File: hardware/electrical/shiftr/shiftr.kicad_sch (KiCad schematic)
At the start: 1 part

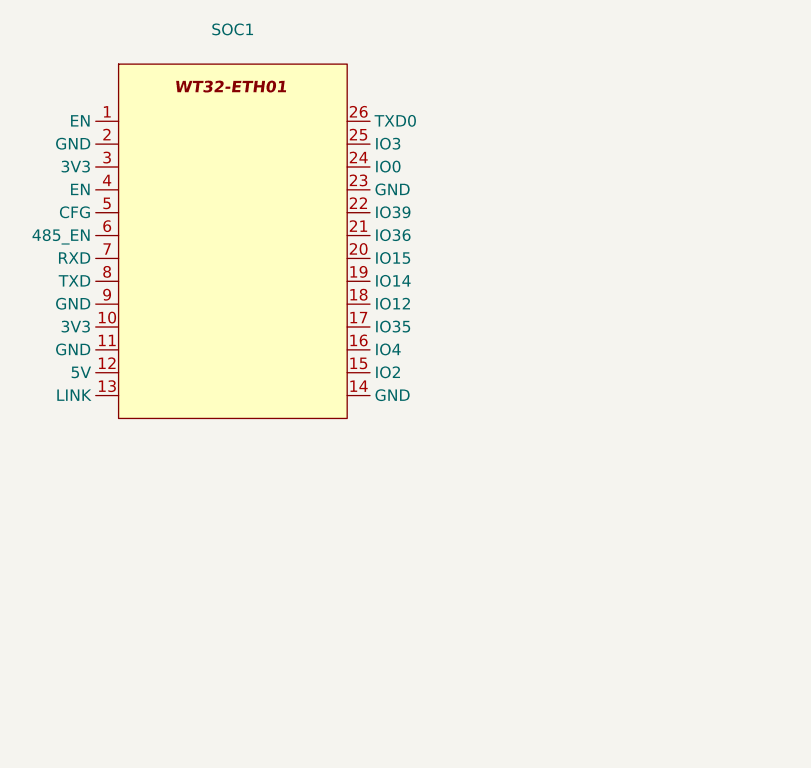
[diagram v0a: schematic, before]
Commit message: add audio jack sch and pcb
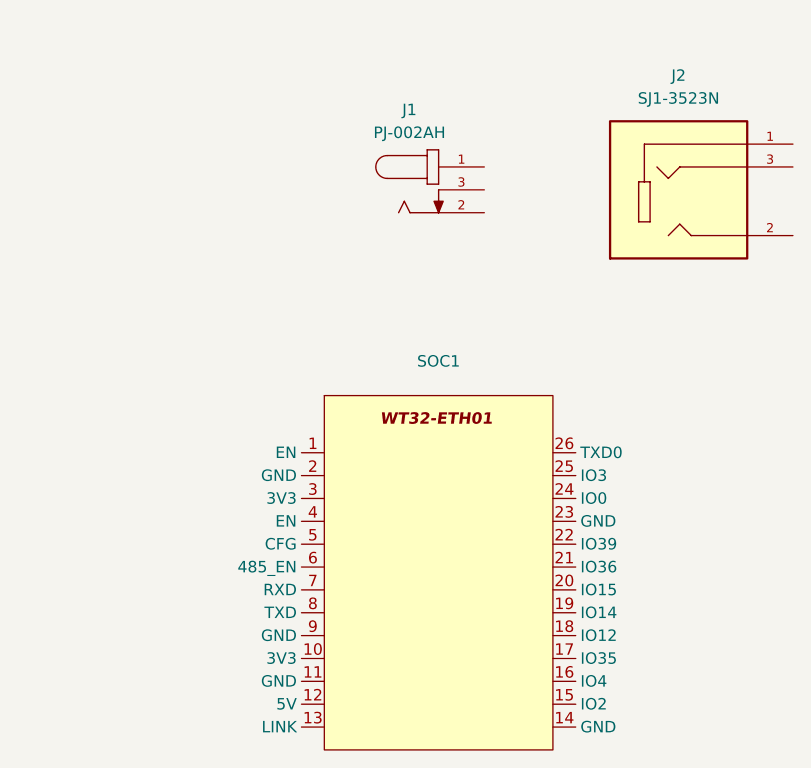
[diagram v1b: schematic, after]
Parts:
- added J1: PJ-002AH, footprint_library:PJ-002AH, symbol symbol_library:PJ-002AH
- added J2: SJ1-3523N, footprint_library:CUI_SJ1-3523N, symbol symbol_library:SJ1-3523N
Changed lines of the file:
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@@
 	(paper "A4")
 	(symbol
+		(lib_id "symbol_library:PJ-002AH")
+		(at 69.85 45.72 0)
+		(unit 1)
+		(exclude_from_sim no)
+		(in_bom yes)
+		(on_board yes)
+		(dnp no)
+		(fields_autoplaced yes)
+		(property "Reference" "J1"
+			(at 66.6143 36.83 0)
+			(effects
+				(font
+					(size 1.27 1.27)
+				)
+			)
+		)
+		(property "Value" "PJ-002AH"
+			(at 66.6143 39.37 0)
+			(effects
+				(font
+					(size 1.27 1.27)
+				)
+			)
+		)
+		(property "Footprint" "footprint_library:PJ-002AH"
+			(at 72.898 58.166 0)
+			(effects
+				(font
+					(size 1.27 1.27)
+				)
+				(justify bottom)
+				(hide yes)
+			)
+		)
+		(property "Datasheet" "https://www.sameskydevices.com/product/resource/pj-002ah.pdf"
+			(at 73.66 36.83 0)
+			(effects
+				(font
+					(size 1.27 1.27)
+				)
+				(hide yes)
+			)
+		)
+		(property "Description" "BARREL JACK 2.1 X 5.5"
+			(at 71.374 34.544 0)
+			(effects
+				(font
+					(size 1.27 1.27)
+				)
+				(hide yes)
+			)
+		)
+		(property "MANUFACTURER" "CUI INC"
+			(at 72.898 54.61 0)
+			(effects
+				(font
+					(size 1.27 1.27)
+				)
+				(justify bottom)
+				(hide yes)
+			)
+		)
+		(property "STANDARD" "Manufacturer recommendations"
+			(at 72.39 56.134 0)
+			(effects
+				(font
+					(size 1.27 1.27)
+				)
+				(justify bottom)
+				(hide yes)
+			)
+		)
+		(pin "1"
+		)
+		(pin "2"
+		)
+		(pin "3"
+		)
+		(instances
+			(project ""
+				(path "/3bfa63c6-9d72-4aec-ae9c-b2577824d50b"
+					(reference "J1")
+					(unit 1)
+				)
+			)
+		)
+	)
+	(symbol
+		(lib_id "symbol_library:SJ1-3523N")
+		(at 96.52 45.72 0)
+		(unit 1)
+		(exclude_from_sim no)
+		(in_bom yes)
+		(on_board yes)
+		(dnp no)
+		(fields_autoplaced yes)
+		(property "Reference" "J2"
+			(at 96.52 33.02 0)
+			(effects
+				(font
+					(size 1.27 1.27)
+				)
+			)
+		)
+		(property "Value" "SJ1-3523N"
+			(at 96.52 35.56 0)
+			(effects
+				(font
+					(size 1.27 1.27)
+				)
+			)
+		)
+		(property "Footprint" "footprint_library:CUI_SJ1-3523N"
+			(at 101.854 59.436 0)
+			(effects
+				(font
+					(size 1.27 1.27)
+				)
+				(justify bottom)
+				(hide yes)
+			)
+		)
+		(property "Datasheet" "https://www.sameskydevices.com/product/resource/sj1-352xn.pdf"
+			(at 96.012 67.818 0)
+			(effects
+				(font
+					(size 1.27 1.27)
+				)
+				(hide yes)
+			)
+		)
+		(property "Description" "AUDIO JACK 3.5MM 3P"
+			(at 96.52 45.72 0)
+			(effects
+				(font
+					(size 1.27 1.27)
+				)
+				(hide yes)
+			)
+		)
+		(property "PARTREV" "1.05"
+			(at 97.028 64.008 0)
+			(effects
+				(font
+					(size 1.27 1.27)
+				)
+				(justify bottom)
+				(hide yes)
+			)
+		)
+		(property "STANDARD" "Manufacturer Recommendations"
+			(at 97.282 57.658 0)
+			(effects
+				(font
+					(size 1.27 1.27)
+				)
+				(justify bottom)
+				(hide yes)
+			)
+		)
+		(property "MAXIMUM_PACKAGE_HEIGHT" "6.25 mm"
+			(at 97.282 66.294 0)
+			(effects
+				(font
+					(size 1.27 1.27)
+				)
+				(justify bottom)
+				(hide yes)
+			)
+		)
+		(property "MANUFACTURER" "CUI Devices"
+			(at 96.774 62.484 0)
+			(effects
+				(font
+					(size 1.27 1.27)
+				)
+				(justify bottom)
+				(hide yes)
+			)
+		)
+		(pin "1"
+		)
+		(pin "3"
+		)
+		(pin "2"
+		)
+		(instances
+			(project ""
+				(path "/3bfa63c6-9d72-4aec-ae9c-b2577824d50b"
+					(reference "J2")
+					(unit 1)
+				)
+			)
+		)
+	)
+	(symbol
 		(lib_id "symbol_library:WT32-ETH01")
-		(at 46.99 59.69 0)
+		(at 69.85 96.52 0)
 		(unit 1)
 		(exclude_from_sim no)
@@
 		(fields_autoplaced yes)
 		(property "Reference" "SOC1"
-			(at 46.99 27.94 0)
+			(at 69.85 64.77 0)
 			(effects
 				(font
@@
 		)
 		(property "Value" "~"
-			(at 46.99 30.48 0)
+			(at 69.85 67.31 0)
 			(effects
 				(font
@@
 		)
 		(property "Footprint" "footprint_library:WT32-ETH01"
-			(at 46.99 59.69 0)
+			(at 69.85 96.52 0)
 			(effects
 				(font
@@
 		)
 		(property "Datasheet" "kicad-embed://WT32-ETH01_datasheet_V1.1- en.pdf"
-			(at 46.99 59.69 0)
-			(effects
-				(font
-					(size 1.27 1.27)
-				)
-				(hide yes)
-			)
-		)
-		(property "Description" ""
-			(at 46.99 59.69 0)
-			(effects
-				(font
-					(size 1.27 1.27)
-				)
-				(hide yes)
-			)
+			(at 69.85 96.52 0)
+			(effects
+				(font
+					(size 1.27 1.27)
+				)
+				(hide yes)
+			)
+		)
+		(property "Description" "ARDUINO"
+			(at 69.85 96.52 0)
+			(effects
+				(font
+					(size 1.27 1.27)
+				)
+				(hide yes)
+			)
+		)
+		(pin "21"
+		)
+		(pin "1"
+		)
+		(pin "3"
+		)
+		(pin "2"
+		)
+		(pin "10"
+		)
+		(pin "13"
+		)
+		(pin "25"
+		)
+		(pin "23"
+		)
+		(pin "11"
+		)
+		(pin "9"
+		)
+		(pin "24"
 		)
 		(pin "22"
 		)
+		(pin "4"
+		)
+		(pin "6"
+		)
+		(pin "7"
+		)
+		(pin "5"
+		)
+		(pin "8"
+		)
+		(pin "12"
+		)
+		(pin "26"
+		)
 		(pin "19"
 		)
-		(pin "21"
-		)
-		(pin "26"
-		)
-		(pin "23"
-		)
-		(pin "2"
-		)
-		(pin "7"
-		)
-		(pin "10"
-		)
-		(pin "9"
+		(pin "17"
+		)
+		(pin "18"
 		)
 		(pin "16"
 		)
-		(pin "11"
-		)
-		(pin "24"
-		)
-		(pin "3"
-		)
-		(pin "12"
-		)
-		(pin "18"
-		)
-		(pin "5"
+		(pin "15"
+		)
+		(pin "20"
 		)
 		(pin "14"
 		)
-		(pin "20"
-		)
-		(pin "6"
-		)
-		(pin "25"
-		)
-		(pin "4"
-		)
-		(pin "17"
-		)
-		(pin "1"
-		)
-		(pin "15"
-		)
-		(pin "8"
-		)
-		(pin "13"
-		)
 		(instances

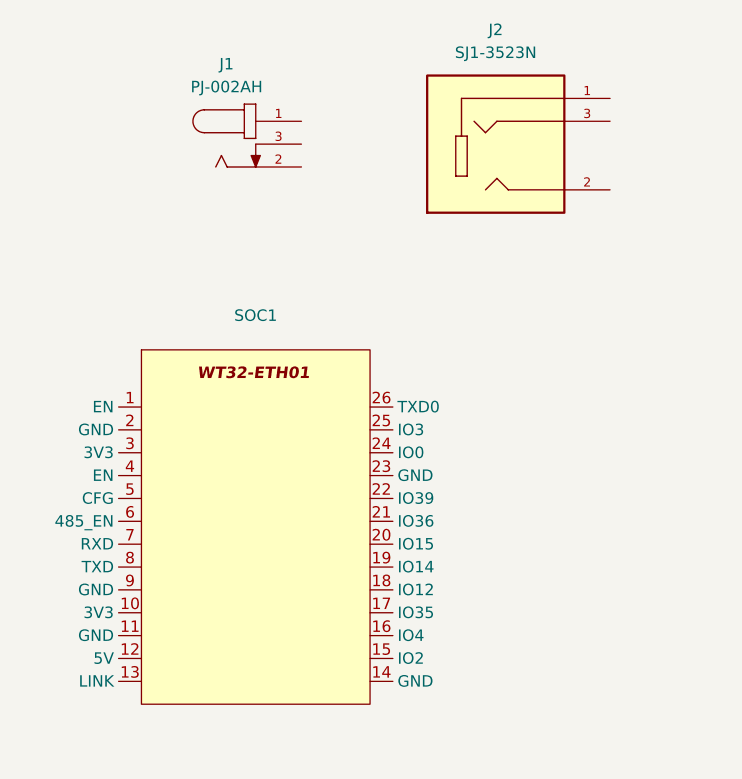
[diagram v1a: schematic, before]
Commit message: add usb c connector sch and pcb lib
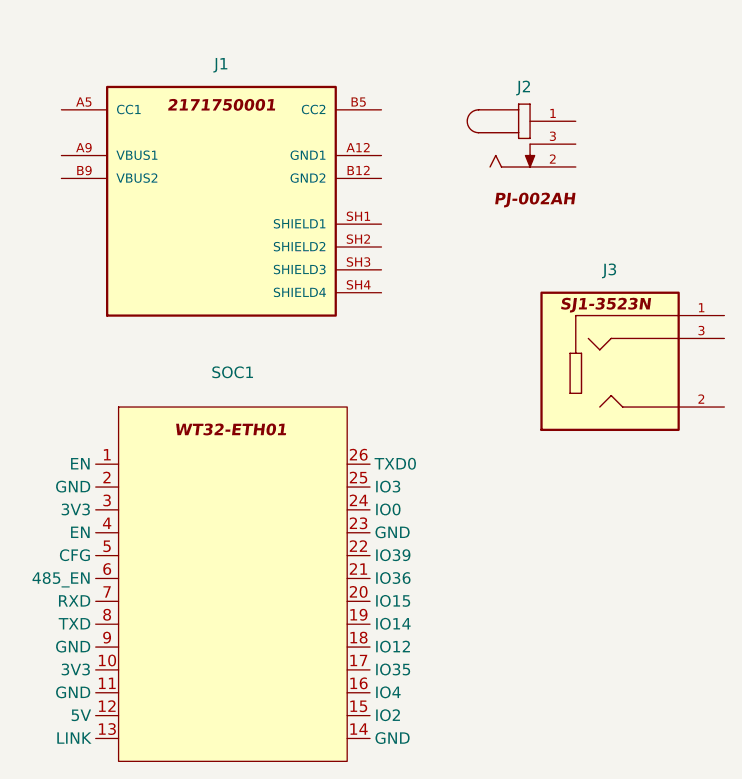
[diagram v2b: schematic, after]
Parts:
- removed J1: PJ-002AH, footprint_library:PJ-002AH, symbol symbol_library:PJ-002AH
- removed J2: SJ1-3523N, footprint_library:CUI_SJ1-3523N, symbol symbol_library:SJ1-3523N
- added J1: 2171750001, footprint_library:MOLEX_2171750001, symbol symbol_library:2171750001
- added J2: PJ-002AH, footprint_library:PJ-002AH, symbol symbol_library:PJ-002AH
- added J3: SJ1-3523N, footprint_library:CUI_SJ1-3523N, symbol symbol_library:SJ1-3523N

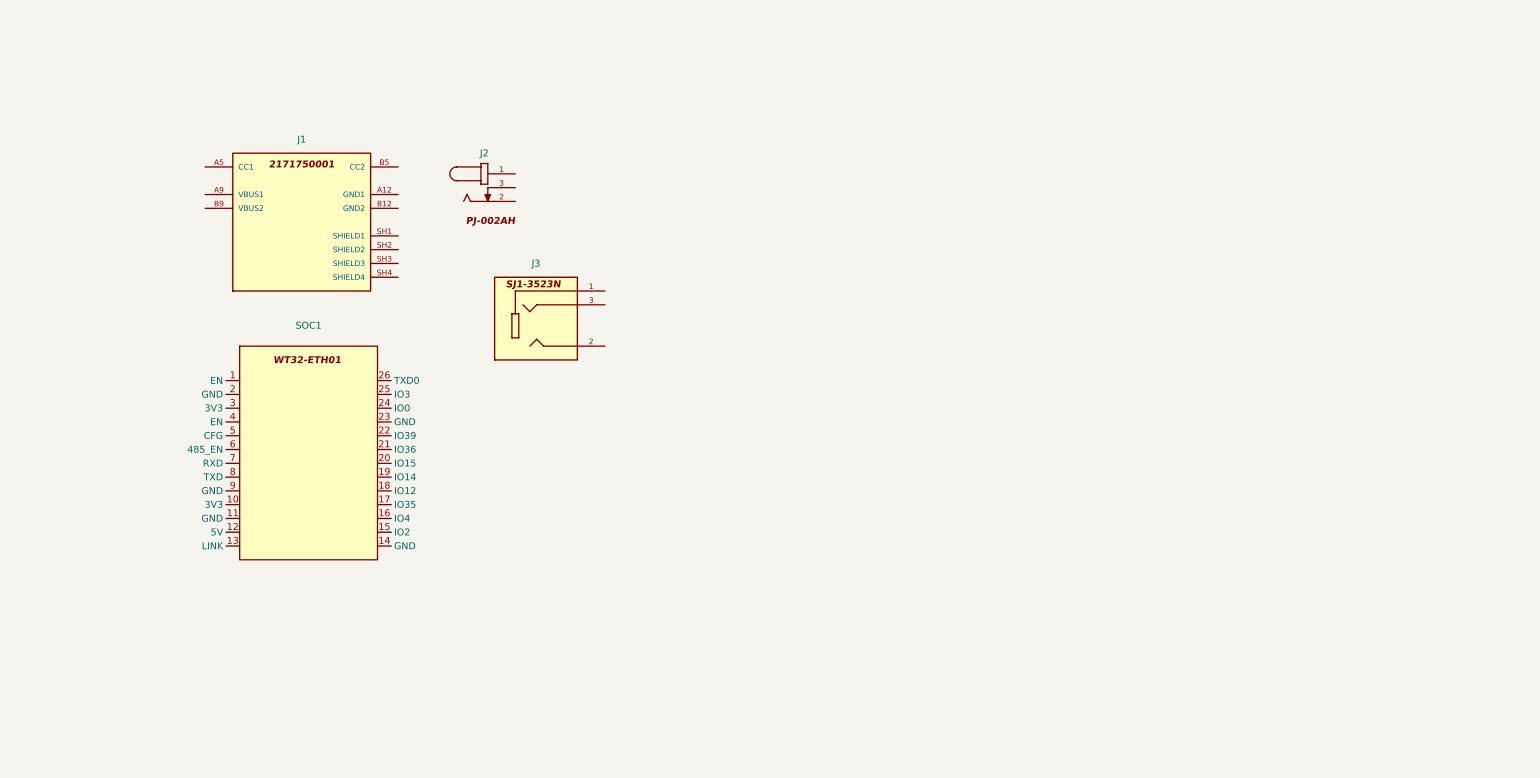
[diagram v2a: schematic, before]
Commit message: add 5.1kohm resistor sch
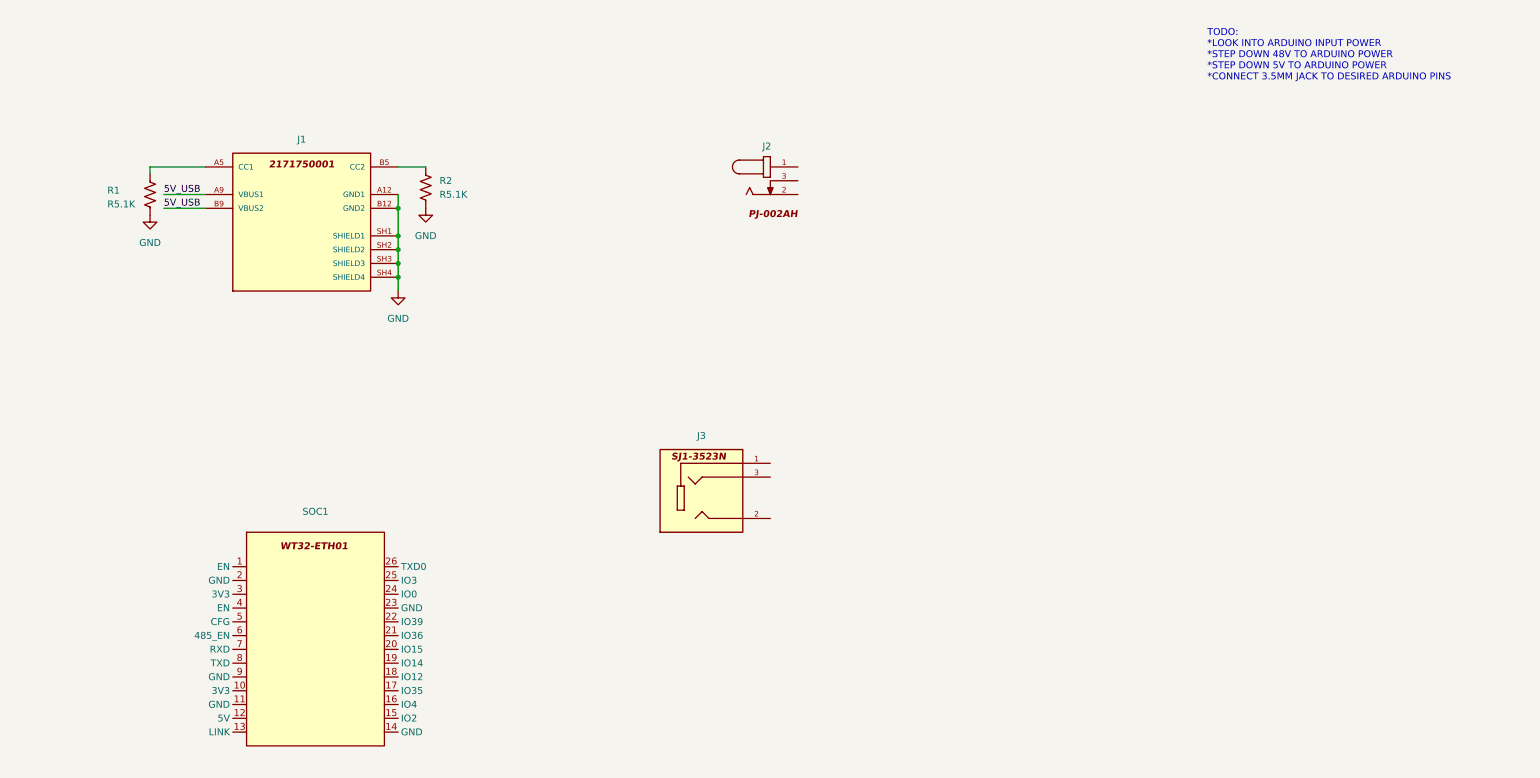
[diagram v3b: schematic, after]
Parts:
- added R1, R2: R5.1K, Resistor_SMD:R_1206_3216Metric, symbol symbol_library:R5.1K
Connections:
- net GND: now reaches J1.A12 (GND1)
- net GND: now also J1.B12 (GND2), J1.SH1 (SHIELD1), J1.SH2 (SHIELD2), J1.SH3 (SHIELD3), J1.SH4 (SHIELD4), R1.2, R2.2
- net at J1.A5 (CC1): now also R1.1
- net 5V_USB: now reaches J1.A9 (VBUS1)
- net 5V_USB: now also J1.B9 (VBUS2)
- net at J1.B5 (CC2): now also R2.1
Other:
- note added: "TODO: *LOOK INTO ARDUINO INPUT POWER *STEP DOWN 48V TO ARDUINO POWER *STEP DOWN 5V TO ARDUINO POWER *CONNECT 3.5MM JACK TO DESIRED ARDUINO PINS"
- moved on the sheet: J2, J3, SOC1

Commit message: flesh out more of the 48v->5v conversion
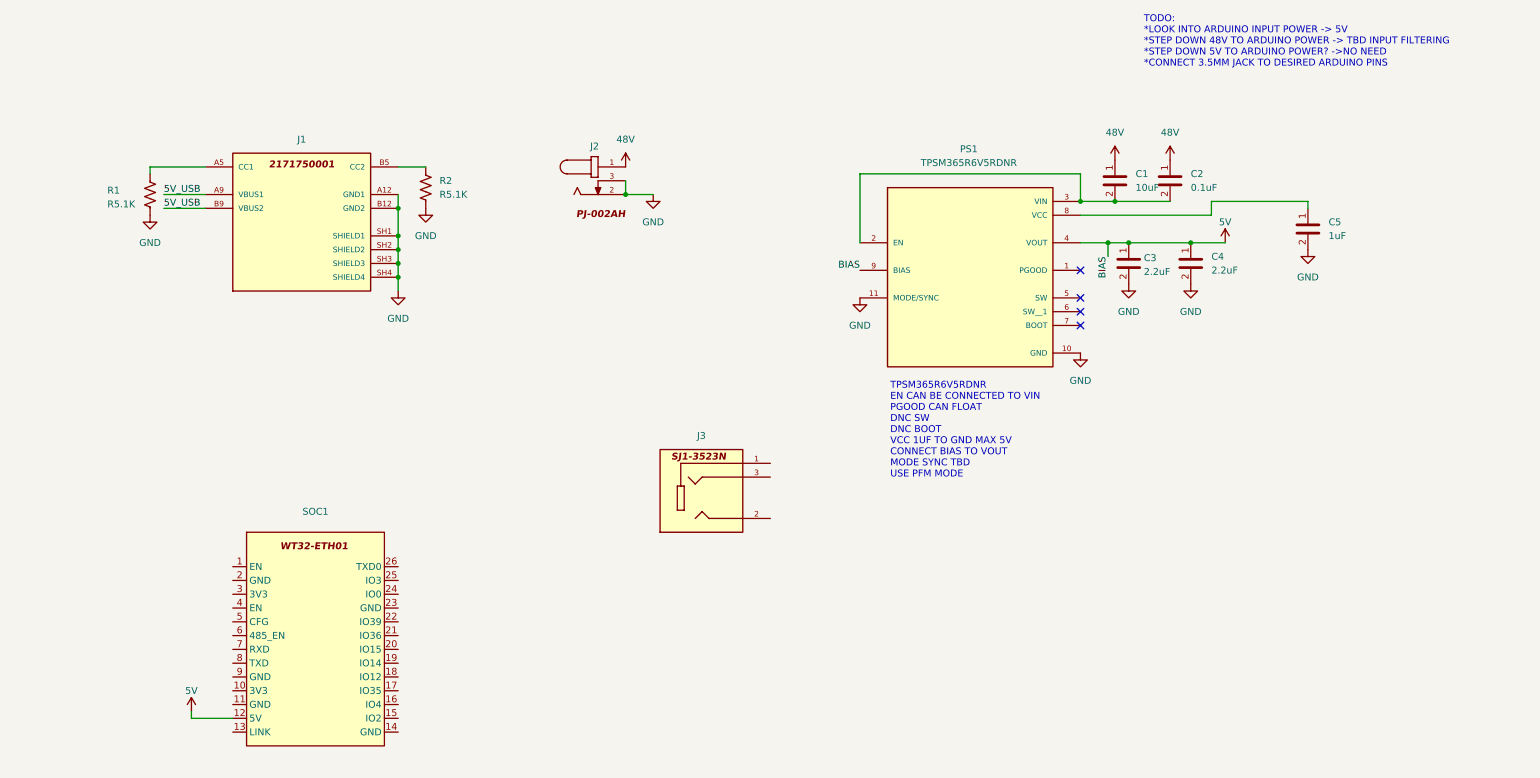
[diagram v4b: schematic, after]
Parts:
- added C1: 10uF, Capacitor_SMD:C_1210_3225Metric, symbol symbol_library:C10uF
- added C2: 0.1uF, Capacitor_SMD:C_1210_3225Metric, symbol symbol_library:C0.1uF
- added C3, C4: 2.2uF, Capacitor_SMD:C_1210_3225Metric, symbol symbol_library:C2.2uF
- added C5: 1uF, Capacitor_SMD:C_0603_1608Metric, symbol symbol_library:C1uF
- added PS1: TPSM365R6V5RDNR, footprint_library:TPSM365R6V5RDNR, symbol symbol_library:TPSM365R6V5RDNR
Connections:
- net GND: now also J2.2, J2.3, C3.2, C4.2, C5.2, PS1.10 (GND), PS1.11 (MODE/SYNC)
- net 48V: now reaches J2.1
- net 48V: now also C1.1, C2.1
- net 5V: now reaches SOC1.12 (5V)
- net 5V: now also C3.1, C4.1, PS1.4 (VOUT), PS1.9 (BIAS)
- new net: C1.2, C2.2, PS1.2 (EN), PS1.3 (VIN)
- new net: C5.1, PS1.8 (VCC)
- no-connect marks 0 -> 4
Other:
- note added: "TODO: *LOOK INTO ARDUINO INPUT POWER -> 5V *STEP DOWN 48V TO ARDUINO POWER -> TBD INPUT FILTERING *STEP DOWN 5V TO ARDUINO POWER? ->NO NEED *CONNECT 3.5MM JACK TO DESIRED ARDUINO PINS"
- note added: "TPSM365R6V5RDNR EN CAN BE CONNECTED TO VIN PGOOD CAN FLOAT DNC SW DNC BOOT VCC 1UF TO GND MAX 5V CONNECT BIAS TO VOUT MODE SYNC TBD USE PFM MODE"
- note removed: "TODO: *LOOK INTO ARDUINO INPUT POWER *STEP DOWN 48V TO ARDUINO POWER *STEP DOWN 5V TO ARDUINO POWER *CONNECT 3.5MM JACK TO DESIRED ARDUINO PINS"
- moved on the sheet: J2, SOC1
